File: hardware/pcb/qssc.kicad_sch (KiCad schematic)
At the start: 113 parts, among them J1 FT232RL, J10 USB-C, J11 Samtec LSHM-130, J2 5V Barrel, J3 SMA, J7 RESET, J8 MW_GATE, J9 JTAG, U1 XC7A35T-1CPG236C, U3 ADF4351BCPZ, U5 GVA-84+, U8 W25Q128JVSIQ, Y1 100MHz TCXO

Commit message: pcb: place 64-ch TIA/comparator front-end + 64-ch P-MOS emitter driver (Phase 1b, DRC 0/0/0)
Board widened 200 -> 210x140. 587 components: 16x TLV9004 TIA + 16x LMV339
comparator (8 cols @ 8mm in the right zone, sized to 2x the TSSOP-14 courtyard
half-extent 3.85mm -- the prior 6.5mm col spacing overlapped adjacent IC pads),
64x Rf/Cf TIA feedback, 64x Rpu comparator pull-up, MCP4725 threshold DAC +
I2C refs; 64x AO3401A P-MOS + 64x Re/64x Rg emitter driver + 8x 74HCT240 buffers
+ decoupling. Re/Rg y-staggered (same x-cols, +3mm y) -- the earlier x-interleave
shorted each Rg +5V pad into the next Re's em_drain pad (56 shorts). J3 SMA ->
x204 right edge, J8 -> (150,8).

ERC 0 errors (775 warnings: the intentional dangling 128 nets + off-grid pins).
DRC 0 violations / 0 unconnected. tests/test_pcb_drc.py passes. 128 nets still
dangle at the die until Phase 2 (FPGA CSG324).

Co-Authored-By: Claude Code <noreply@anthropic.com>
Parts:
- removed C66: 100nF, Capacitor_SMD:C_0603_1608Metric, symbol qssc:C
- removed J11: Samtec LSHM-130, Connector_Samtec:Samtec_LSHM-130-xx.x-x-DV-N_2x30_P0.50mm_Vertical, symbol qssc:Conn_02x30_Odd_Even
- removed R84: 47k, Resistor_SMD:R_0603_1608Metric, symbol qssc:R
- removed R85: 10k, Resistor_SMD:R_0603_1608Metric, symbol qssc:R
- added Cdac, Cref, Cub0, Cub1, Cub2, Cub3, Cub4, Cub5, Cub6, Cub7, Cuc0, Cuc1, Cuc10, Cuc11, Cuc12, Cuc13, Cuc14, Cuc15, Cuc2, Cuc3, Cuc4, Cuc5, Cuc6, Cuc7, Cuc8, Cuc9, Cut0, Cut1, Cut10, Cut11, Cut12, Cut13, Cut14, Cut15, Cut2, Cut3, Cut4, Cut5, Cut6, Cut7, Cut8, Cut9: 100nF, Capacitor_SMD:C_0603_1608Metric, symbol qssc:C
- added Cf0, Cf1, Cf10, Cf11, Cf12, Cf13, Cf14, Cf15, Cf16, Cf17, Cf18, Cf19, Cf2, Cf20, Cf21, Cf22, Cf23, Cf24, Cf25, Cf26, Cf27, Cf28, Cf29, Cf3, Cf30, Cf31, Cf32, Cf33, Cf34, Cf35, Cf36, Cf37, Cf38, Cf39, Cf4, Cf40, Cf41, Cf42, Cf43, Cf44, Cf45, Cf46, Cf47, Cf48, Cf49, Cf5, Cf50, Cf51, Cf52, Cf53, Cf54, Cf55, Cf56, Cf57, Cf58, Cf59, Cf6, Cf60, Cf61, Cf62, Cf63, Cf7, Cf8, Cf9: 1pF, Capacitor_SMD:C_0603_1608Metric, symbol qssc:C
- added Q0, Q1, Q10, Q11, Q12, Q13, Q14, Q15, Q16, Q17, Q18, Q19, Q2, Q20, Q21, Q22, Q23, Q24, Q25, Q26, Q27, Q28, Q29, Q3, Q30, Q31, Q32, Q33, Q34, Q35, Q36, Q37, Q38, Q39, Q4, Q40, Q41, Q42, Q43, Q44, Q45, Q46, Q47, Q48, Q49, Q5, Q50, Q51, Q52, Q53, Q54, Q55, Q56, Q57, Q58, Q59, Q6, Q60, Q61, Q62, Q63, Q7, Q8, Q9: AO3401A, Package_TO_SOT_SMD:SOT-23, symbol qssc:AO3401A
- added R_I2C_SCL, R_I2C_SDA: 4.7k, Resistor_SMD:R_0603_1608Metric, symbol qssc:R
- added Re0, Re1, Re10, Re11, Re12, Re13, Re14, Re15, Re16, Re17, Re18, Re19, Re2, Re20, Re21, Re22, Re23, Re24, Re25, Re26, Re27, Re28, Re29, Re3, Re30, Re31, Re32, Re33, Re34, Re35, Re36, Re37, Re38, Re39, Re4, Re40, Re41, Re42, Re43, Re44, Re45, Re46, Re47, Re48, Re49, Re5, Re50, Re51, Re52, Re53, Re54, Re55, Re56, Re57, Re58, Re59, Re6, Re60, Re61, Re62, Re63, Re7, Re8, Re9: 220R, Resistor_SMD:R_0603_1608Metric, symbol qssc:R
- added Rf0, Rf1, Rf10, Rf11, Rf12, Rf13, Rf14, Rf15, Rf16, Rf17, Rf18, Rf19, Rf2, Rf20, Rf21, Rf22, Rf23, Rf24, Rf25, Rf26, Rf27, Rf28, Rf29, Rf3, Rf30, Rf31, Rf32, Rf33, Rf34, Rf35, Rf36, Rf37, Rf38, Rf39, Rf4, Rf40, Rf41, Rf42, Rf43, Rf44, Rf45, Rf46, Rf47, Rf48, Rf49, Rf5, Rf50, Rf51, Rf52, Rf53, Rf54, Rf55, Rf56, Rf57, Rf58, Rf59, Rf6, Rf60, Rf61, Rf62, Rf63, Rf7, Rf8, Rf9: 1M, Resistor_SMD:R_0603_1608Metric, symbol qssc:R
- added Rg0, Rg1, Rg10, Rg11, Rg12, Rg13, Rg14, Rg15, Rg16, Rg17, Rg18, Rg19, Rg2, Rg20, Rg21, Rg22, Rg23, Rg24, Rg25, Rg26, Rg27, Rg28, Rg29, Rg3, Rg30, Rg31, Rg32, Rg33, Rg34, Rg35, Rg36, Rg37, Rg38, Rg39, Rg4, Rg40, Rg41, Rg42, Rg43, Rg44, Rg45, Rg46, Rg47, Rg48, Rg49, Rg5, Rg50, Rg51, Rg52, Rg53, Rg54, Rg55, Rg56, Rg57, Rg58, Rg59, Rg6, Rg60, Rg61, Rg62, Rg63, Rg7, Rg8, Rg9: 100k, Resistor_SMD:R_0603_1608Metric, symbol qssc:R
- added Rpu0, Rpu1, Rpu10, Rpu11, Rpu12, Rpu13, Rpu14, Rpu15, Rpu16, Rpu17, Rpu18, Rpu19, Rpu2, Rpu20, Rpu21, Rpu22, Rpu23, Rpu24, Rpu25, Rpu26, Rpu27, Rpu28, Rpu29, Rpu3, Rpu30, Rpu31, Rpu32, Rpu33, Rpu34, Rpu35, Rpu36, Rpu37, Rpu38, Rpu39, Rpu4, Rpu40, Rpu41, Rpu42, Rpu43, Rpu44, Rpu45, Rpu46, Rpu47, Rpu48, Rpu49, Rpu5, Rpu50, Rpu51, Rpu52, Rpu53, Rpu54, Rpu55, Rpu56, Rpu57, Rpu58, Rpu59, Rpu6, Rpu60, Rpu61, Rpu62, Rpu63, Rpu7, Rpu8, Rpu9, Rref1, Rref2: 10k, Resistor_SMD:R_0603_1608Metric, symbol qssc:R
- added UB0, UB1, UB2, UB3, UB4, UB5, UB6, UB7: 74HCT240, Package_SO:TSSOP-20_4.4x6.5mm_P0.65mm, symbol qssc:74HCT240
- added UC0, UC1, UC10, UC11, UC12, UC13, UC14, UC15, UC2, UC3, UC4, UC5, UC6, UC7, UC8, UC9: LMV339, Package_SO:SOIC-14_3.9x8.7mm_P1.27mm, symbol qssc:LMV339
- added UDAC: MCP4725, Package_TO_SOT_SMD:SOT-23-6, symbol qssc:MCP4725
- added UT0, UT1, UT10, UT11, UT12, UT13, UT14, UT15, UT2, UT3, UT4, UT5, UT6, UT7, UT8, UT9: TLV9004, Package_SO:TSSOP-14_4.4x5mm_P0.65mm, symbol qssc:TLV9004
- added Uchip: QSSC_Chip, qssc:QSSC_Chip, symbol qssc:QSSC_Chip
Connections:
- net +3V3: now also Cuc0.1, Cuc1.1, Cuc10.1, Cuc11.1, Cuc12.1, Cuc13.1, Cuc14.1, Cuc15.1, Cuc2.1, Cuc3.1, Cuc4.1, Cuc5.1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
- net +5V: now also Cub0.1, Cub1.1, Cub2.1, Cub3.1, Cub4.1, Cub5.1, Cub6.1, Cub7.1, Q0.2 (S), Q1.2 (S), Q10.2 (S), Q11.2 (S)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
- net GND: now also Cdac.2, Cref.2, Cub0.2, Cub1.2, Cub2.2, Cub3.2, Cub4.2, Cub5.2, Cub6.2, Cub7.2, Cuc0.2, Cuc1.2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; no longer U1.B13 (GND)
- removed net TIA_ADC: U1.A12 (TIA_ADC)
- new net DET_DIG0: Rpu0.1, UC0.1 (OUTA)
- new net DET_DIG1: Rpu1.1, UC0.6 (OUTB)
- new net DET_DIG10: Rpu10.1, UC2.8 (OUTC)
- new net DET_DIG11: Rpu11.1, UC2.11 (OUTD)
- new net DET_DIG12: Rpu12.1, UC3.1 (OUTA)
- new net DET_DIG13: Rpu13.1, UC3.6 (OUTB)
- new net DET_DIG14: Rpu14.1, UC3.8 (OUTC)
- new net DET_DIG15: Rpu15.1, UC3.11 (OUTD)
- new net DET_DIG16: Rpu16.1, UC4.1 (OUTA)
- new net DET_DIG17: Rpu17.1, UC4.6 (OUTB)
- new net DET_DIG18: Rpu18.1, UC4.8 (OUTC)
- new net DET_DIG19: Rpu19.1, UC4.11 (OUTD)
- new net DET_DIG2: Rpu2.1, UC0.8 (OUTC)
- new net DET_DIG20: Rpu20.1, UC5.1 (OUTA)
- new net DET_DIG21: Rpu21.1, UC5.6 (OUTB)
- new net DET_DIG22: Rpu22.1, UC5.8 (OUTC)
- new net DET_DIG23: Rpu23.1, UC5.11 (OUTD)
- new net DET_DIG24: Rpu24.1, UC6.1 (OUTA)
- new net DET_DIG25: Rpu25.1, UC6.6 (OUTB)
- new net DET_DIG26: Rpu26.1, UC6.8 (OUTC)
- new net DET_DIG27: Rpu27.1, UC6.11 (OUTD)
- new net DET_DIG28: Rpu28.1, UC7.1 (OUTA)
- new net DET_DIG29: Rpu29.1, UC7.6 (OUTB)
- new net DET_DIG3: Rpu3.1, UC0.11 (OUTD)
- new net DET_DIG30: Rpu30.1, UC7.8 (OUTC)
- new net DET_DIG31: Rpu31.1, UC7.11 (OUTD)
- new net DET_DIG32: Rpu32.1, UC8.1 (OUTA)
- new net DET_DIG33: Rpu33.1, UC8.6 (OUTB)
- new net DET_DIG34: Rpu34.1, UC8.8 (OUTC)
- new net DET_DIG35: Rpu35.1, UC8.11 (OUTD)
- new net DET_DIG36: Rpu36.1, UC9.1 (OUTA)
- new net DET_DIG37: Rpu37.1, UC9.6 (OUTB)
- new net DET_DIG38: Rpu38.1, UC9.8 (OUTC)
- new net DET_DIG39: Rpu39.1, UC9.11 (OUTD)
- new net DET_DIG4: Rpu4.1, UC1.1 (OUTA)
- new net DET_DIG40: Rpu40.1, UC10.1 (OUTA)
- new net DET_DIG41: Rpu41.1, UC10.6 (OUTB)
- new net DET_DIG42: Rpu42.1, UC10.8 (OUTC)
- new net DET_DIG43: Rpu43.1, UC10.11 (OUTD)
- new net DET_DIG44: Rpu44.1, UC11.1 (OUTA)
- new net DET_DIG45: Rpu45.1, UC11.6 (OUTB)
- new net DET_DIG46: Rpu46.1, UC11.8 (OUTC)
- new net DET_DIG47: Rpu47.1, UC11.11 (OUTD)
- new net DET_DIG48: Rpu48.1, UC12.1 (OUTA)
- new net DET_DIG49: Rpu49.1, UC12.6 (OUTB)
- new net DET_DIG5: Rpu5.1, UC1.6 (OUTB)
- new net DET_DIG50: Rpu50.1, UC12.8 (OUTC)
- new net DET_DIG51: Rpu51.1, UC12.11 (OUTD)
- new net DET_DIG52: Rpu52.1, UC13.1 (OUTA)
- new net DET_DIG53: Rpu53.1, UC13.6 (OUTB)
- new net DET_DIG54: Rpu54.1, UC13.8 (OUTC)
- new net DET_DIG55: Rpu55.1, UC13.11 (OUTD)
- new net DET_DIG56: Rpu56.1, UC14.1 (OUTA)
- new net DET_DIG57: Rpu57.1, UC14.6 (OUTB)
- new net DET_DIG58: Rpu58.1, UC14.8 (OUTC)
- new net DET_DIG59: Rpu59.1, UC14.11 (OUTD)
- new net DET_DIG6: Rpu6.1, UC1.8 (OUTC)
- new net DET_DIG60: Rpu60.1, UC15.1 (OUTA)
- new net DET_DIG61: Rpu61.1, UC15.6 (OUTB)
- new net DET_DIG62: Rpu62.1, UC15.8 (OUTC)
- new net DET_DIG63: Rpu63.1, UC15.11 (OUTD)
- new net DET_DIG7: Rpu7.1, UC1.11 (OUTD)
- new net DET_DIG8: Rpu8.1, UC2.1 (OUTA)
- new net DET_DIG9: Rpu9.1, UC2.6 (OUTB)
- new net DET_IN0: Cf0.1, Rf0.1, UT0.2 (INA-), Uchip.DET0
- new net DET_IN1: Cf1.1, Rf1.1, UT0.6 (INB-), Uchip.DET1
- new net DET_IN10: Cf10.1, Rf10.1, UT2.9 (INC-), Uchip.DET10
- new net DET_IN11: Cf11.1, Rf11.1, UT2.13 (IND-), Uchip.DET11
- new net DET_IN12: Cf12.1, Rf12.1, UT3.2 (INA-), Uchip.DET12
- new net DET_IN13: Cf13.1, Rf13.1, UT3.6 (INB-), Uchip.DET13
- new net DET_IN14: Cf14.1, Rf14.1, UT3.9 (INC-), Uchip.DET14
- new net DET_IN15: Cf15.1, Rf15.1, UT3.13 (IND-), Uchip.DET15
- new net DET_IN16: Cf16.1, Rf16.1, UT4.2 (INA-), Uchip.DET16
- new net DET_IN17: Cf17.1, Rf17.1, UT4.6 (INB-), Uchip.DET17
- new net DET_IN18: Cf18.1, Rf18.1, UT4.9 (INC-), Uchip.DET18
- new net DET_IN19: Cf19.1, Rf19.1, UT4.13 (IND-), Uchip.DET19
- new net DET_IN2: Cf2.1, Rf2.1, UT0.9 (INC-), Uchip.DET2
- new net DET_IN20: Cf20.1, Rf20.1, UT5.2 (INA-), Uchip.DET20
- new net DET_IN21: Cf21.1, Rf21.1, UT5.6 (INB-), Uchip.DET21
- new net DET_IN22: Cf22.1, Rf22.1, UT5.9 (INC-), Uchip.DET22
- new net DET_IN23: Cf23.1, Rf23.1, UT5.13 (IND-), Uchip.DET23
- new net DET_IN24: Cf24.1, Rf24.1, UT6.2 (INA-), Uchip.DET24
- new net DET_IN25: Cf25.1, Rf25.1, UT6.6 (INB-), Uchip.DET25
- new net DET_IN26: Cf26.1, Rf26.1, UT6.9 (INC-), Uchip.DET26
- new net DET_IN27: Cf27.1, Rf27.1, UT6.13 (IND-), Uchip.DET27
- new net DET_IN28: Cf28.1, Rf28.1, UT7.2 (INA-), Uchip.DET28
- new net DET_IN29: Cf29.1, Rf29.1, UT7.6 (INB-), Uchip.DET29
- new net DET_IN3: Cf3.1, Rf3.1, UT0.13 (IND-), Uchip.DET3
- new net DET_IN30: Cf30.1, Rf30.1, UT7.9 (INC-), Uchip.DET30
- new net DET_IN31: Cf31.1, Rf31.1, UT7.13 (IND-), Uchip.DET31
- new net DET_IN32: Cf32.1, Rf32.1, UT8.2 (INA-), Uchip.DET32
- new net DET_IN33: Cf33.1, Rf33.1, UT8.6 (INB-), Uchip.DET33
- new net DET_IN34: Cf34.1, Rf34.1, UT8.9 (INC-), Uchip.DET34
- new net DET_IN35: Cf35.1, Rf35.1, UT8.13 (IND-), Uchip.DET35
- new net DET_IN36: Cf36.1, Rf36.1, UT9.2 (INA-), Uchip.DET36
- new net DET_IN37: Cf37.1, Rf37.1, UT9.6 (INB-), Uchip.DET37
- new net DET_IN38: Cf38.1, Rf38.1, UT9.9 (INC-), Uchip.DET38
- new net DET_IN39: Cf39.1, Rf39.1, UT9.13 (IND-), Uchip.DET39
- new net DET_IN4: Cf4.1, Rf4.1, UT1.2 (INA-), Uchip.DET4
- new net DET_IN40: Cf40.1, Rf40.1, UT10.2 (INA-), Uchip.DET40
- new net DET_IN41: Cf41.1, Rf41.1, UT10.6 (INB-), Uchip.DET41
- new net DET_IN42: Cf42.1, Rf42.1, UT10.9 (INC-), Uchip.DET42
- new net DET_IN43: Cf43.1, Rf43.1, UT10.13 (IND-), Uchip.DET43
- new net DET_IN44: Cf44.1, Rf44.1, UT11.2 (INA-), Uchip.DET44
- new net DET_IN45: Cf45.1, Rf45.1, UT11.6 (INB-), Uchip.DET45
- new net DET_IN46: Cf46.1, Rf46.1, UT11.9 (INC-), Uchip.DET46
- new net DET_IN47: Cf47.1, Rf47.1, UT11.13 (IND-), Uchip.DET47
- new net DET_IN48: Cf48.1, Rf48.1, UT12.2 (INA-), Uchip.DET48
- new net DET_IN49: Cf49.1, Rf49.1, UT12.6 (INB-), Uchip.DET49
- new net DET_IN5: Cf5.1, Rf5.1, UT1.6 (INB-), Uchip.DET5
- new net DET_IN50: Cf50.1, Rf50.1, UT12.9 (INC-), Uchip.DET50
- new net DET_IN51: Cf51.1, Rf51.1, UT12.13 (IND-), Uchip.DET51
- new net DET_IN52: Cf52.1, Rf52.1, UT13.2 (INA-), Uchip.DET52
- new net DET_IN53: Cf53.1, Rf53.1, UT13.6 (INB-), Uchip.DET53
- new net DET_IN54: Cf54.1, Rf54.1, UT13.9 (INC-), Uchip.DET54
- new net DET_IN55: Cf55.1, Rf55.1, UT13.13 (IND-), Uchip.DET55
- new net DET_IN56: Cf56.1, Rf56.1, UT14.2 (INA-), Uchip.DET56
- new net DET_IN57: Cf57.1, Rf57.1, UT14.6 (INB-), Uchip.DET57
- new net DET_IN58: Cf58.1, Rf58.1, UT14.9 (INC-), Uchip.DET58
- new net DET_IN59: Cf59.1, Rf59.1, UT14.13 (IND-), Uchip.DET59
- new net DET_IN6: Cf6.1, Rf6.1, UT1.9 (INC-), Uchip.DET6
- new net DET_IN60: Cf60.1, Rf60.1, UT15.2 (INA-), Uchip.DET60
- new net DET_IN61: Cf61.1, Rf61.1, UT15.6 (INB-), Uchip.DET61
- new net DET_IN62: Cf62.1, Rf62.1, UT15.9 (INC-), Uchip.DET62
- new net DET_IN63: Cf63.1, Rf63.1, UT15.13 (IND-), Uchip.DET63
- new net DET_IN7: Cf7.1, Rf7.1, UT1.13 (IND-), Uchip.DET7
- new net DET_IN8: Cf8.1, Rf8.1, UT2.2 (INA-), Uchip.DET8
- new net DET_IN9: Cf9.1, Rf9.1, UT2.6 (INB-), Uchip.DET9
- new net DET_REF: Cref.1, Rref1.2, Rref2.1, UT0.10 (INC+), UT0.12 (IND+), UT0.3 (INA+), UT0.5 (INB+), UT1.10 (INC+), UT1.12 (IND+), UT1.3 (INA+), UT1.5 (INB+), UT10.10 (INC+)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
- new net DET_THR: Cdac.1, UC0.13 (IND-), UC0.2 (INA-), UC0.4 (INB-), UC0.9 (INC-), UC1.13 (IND-), UC1.2 (INA-), UC1.4 (INB-), UC1.9 (INC-), UC10.13 (IND-), UC10.2 (INA-), UC10.4 (INB-)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
- new net DET_TIA0: Cf0.2, Rf0.2, UC0.3 (INA+), UT0.1 (OUTA)
- new net DET_TIA1: Cf1.2, Rf1.2, UC0.5 (INB+), UT0.7 (OUTB)
- new net DET_TIA10: Cf10.2, Rf10.2, UC2.10 (INC+), UT2.8 (OUTC)
- new net DET_TIA11: Cf11.2, Rf11.2, UC2.12 (IND+), UT2.14 (OUTD)
- new net DET_TIA12: Cf12.2, Rf12.2, UC3.3 (INA+), UT3.1 (OUTA)
- new net DET_TIA13: Cf13.2, Rf13.2, UC3.5 (INB+), UT3.7 (OUTB)
- new net DET_TIA14: Cf14.2, Rf14.2, UC3.10 (INC+), UT3.8 (OUTC)
- new net DET_TIA15: Cf15.2, Rf15.2, UC3.12 (IND+), UT3.14 (OUTD)
- new net DET_TIA16: Cf16.2, Rf16.2, UC4.3 (INA+), UT4.1 (OUTA)
- new net DET_TIA17: Cf17.2, Rf17.2, UC4.5 (INB+), UT4.7 (OUTB)
- new net DET_TIA18: Cf18.2, Rf18.2, UC4.10 (INC+), UT4.8 (OUTC)
- new net DET_TIA19: Cf19.2, Rf19.2, UC4.12 (IND+), UT4.14 (OUTD)
- new net DET_TIA2: Cf2.2, Rf2.2, UC0.10 (INC+), UT0.8 (OUTC)
- new net DET_TIA20: Cf20.2, Rf20.2, UC5.3 (INA+), UT5.1 (OUTA)
- new net DET_TIA21: Cf21.2, Rf21.2, UC5.5 (INB+), UT5.7 (OUTB)
- new net DET_TIA22: Cf22.2, Rf22.2, UC5.10 (INC+), UT5.8 (OUTC)
- new net DET_TIA23: Cf23.2, Rf23.2, UC5.12 (IND+), UT5.14 (OUTD)
- new net DET_TIA24: Cf24.2, Rf24.2, UC6.3 (INA+), UT6.1 (OUTA)
- new net DET_TIA25: Cf25.2, Rf25.2, UC6.5 (INB+), UT6.7 (OUTB)
- new net DET_TIA26: Cf26.2, Rf26.2, UC6.10 (INC+), UT6.8 (OUTC)
- new net DET_TIA27: Cf27.2, Rf27.2, UC6.12 (IND+), UT6.14 (OUTD)
- new net DET_TIA28: Cf28.2, Rf28.2, UC7.3 (INA+), UT7.1 (OUTA)
- new net DET_TIA29: Cf29.2, Rf29.2, UC7.5 (INB+), UT7.7 (OUTB)
- new net DET_TIA3: Cf3.2, Rf3.2, UC0.12 (IND+), UT0.14 (OUTD)
- new net DET_TIA30: Cf30.2, Rf30.2, UC7.10 (INC+), UT7.8 (OUTC)
- new net DET_TIA31: Cf31.2, Rf31.2, UC7.12 (IND+), UT7.14 (OUTD)
- new net DET_TIA32: Cf32.2, Rf32.2, UC8.3 (INA+), UT8.1 (OUTA)
- new net DET_TIA33: Cf33.2, Rf33.2, UC8.5 (INB+), UT8.7 (OUTB)
- new net DET_TIA34: Cf34.2, Rf34.2, UC8.10 (INC+), UT8.8 (OUTC)
- new net DET_TIA35: Cf35.2, Rf35.2, UC8.12 (IND+), UT8.14 (OUTD)
- new net DET_TIA36: Cf36.2, Rf36.2, UC9.3 (INA+), UT9.1 (OUTA)
- new net DET_TIA37: Cf37.2, Rf37.2, UC9.5 (INB+), UT9.7 (OUTB)
- new net DET_TIA38: Cf38.2, Rf38.2, UC9.10 (INC+), UT9.8 (OUTC)
- new net DET_TIA39: Cf39.2, Rf39.2, UC9.12 (IND+), UT9.14 (OUTD)
- new net DET_TIA4: Cf4.2, Rf4.2, UC1.3 (INA+), UT1.1 (OUTA)
- new net DET_TIA40: Cf40.2, Rf40.2, UC10.3 (INA+), UT10.1 (OUTA)
- new net DET_TIA41: Cf41.2, Rf41.2, UC10.5 (INB+), UT10.7 (OUTB)
- new net DET_TIA42: Cf42.2, Rf42.2, UC10.10 (INC+), UT10.8 (OUTC)
- new net DET_TIA43: Cf43.2, Rf43.2, UC10.12 (IND+), UT10.14 (OUTD)
- new net DET_TIA44: Cf44.2, Rf44.2, UC11.3 (INA+), UT11.1 (OUTA)
- new net DET_TIA45: Cf45.2, Rf45.2, UC11.5 (INB+), UT11.7 (OUTB)
- new net DET_TIA46: Cf46.2, Rf46.2, UC11.10 (INC+), UT11.8 (OUTC)
- new net DET_TIA47: Cf47.2, Rf47.2, UC11.12 (IND+), UT11.14 (OUTD)
- new net DET_TIA48: Cf48.2, Rf48.2, UC12.3 (INA+), UT12.1 (OUTA)
- new net DET_TIA49: Cf49.2, Rf49.2, UC12.5 (INB+), UT12.7 (OUTB)
- new net DET_TIA5: Cf5.2, Rf5.2, UC1.5 (INB+), UT1.7 (OUTB)
- new net DET_TIA50: Cf50.2, Rf50.2, UC12.10 (INC+), UT12.8 (OUTC)
- new net DET_TIA51: Cf51.2, Rf51.2, UC12.12 (IND+), UT12.14 (OUTD)
- new net DET_TIA52: Cf52.2, Rf52.2, UC13.3 (INA+), UT13.1 (OUTA)
- new net DET_TIA53: Cf53.2, Rf53.2, UC13.5 (INB+), UT13.7 (OUTB)
- new net DET_TIA54: Cf54.2, Rf54.2, UC13.10 (INC+), UT13.8 (OUTC)
- new net DET_TIA55: Cf55.2, Rf55.2, UC13.12 (IND+), UT13.14 (OUTD)
- new net DET_TIA56: Cf56.2, Rf56.2, UC14.3 (INA+), UT14.1 (OUTA)
- new net DET_TIA57: Cf57.2, Rf57.2, UC14.5 (INB+), UT14.7 (OUTB)
- new net DET_TIA58: Cf58.2, Rf58.2, UC14.10 (INC+), UT14.8 (OUTC)
- new net DET_TIA59: Cf59.2, Rf59.2, UC14.12 (IND+), UT14.14 (OUTD)
- new net DET_TIA6: Cf6.2, Rf6.2, UC1.10 (INC+), UT1.8 (OUTC)
- new net DET_TIA60: Cf60.2, Rf60.2, UC15.3 (INA+), UT15.1 (OUTA)
- new net DET_TIA61: Cf61.2, Rf61.2, UC15.5 (INB+), UT15.7 (OUTB)
- new net DET_TIA62: Cf62.2, Rf62.2, UC15.10 (INC+), UT15.8 (OUTC)
- new net DET_TIA63: Cf63.2, Rf63.2, UC15.12 (IND+), UT15.14 (OUTD)
- new net DET_TIA7: Cf7.2, Rf7.2, UC1.12 (IND+), UT1.14 (OUTD)
- new net DET_TIA8: Cf8.2, Rf8.2, UC2.3 (INA+), UT2.1 (OUTA)
- new net DET_TIA9: Cf9.2, Rf9.2, UC2.5 (INB+), UT2.7 (OUTB)
- new net EM_DRV0: UB0.2 (1A0)
- new net EM_DRV1: UB0.4 (1A1)
- new net EM_DRV10: UB1.6 (1A2)
- new net EM_DRV11: UB1.8 (1A3)
- new net EM_DRV12: UB1.17 (2A0)
- new net EM_DRV13: UB1.15 (2A1)
- new net EM_DRV14: UB1.13 (2A2)
- new net EM_DRV15: UB1.11 (2A3)
- new net EM_DRV16: UB2.2 (1A0)
- new net EM_DRV17: UB2.4 (1A1)
- new net EM_DRV18: UB2.6 (1A2)
- new net EM_DRV19: UB2.8 (1A3)
- new net EM_DRV2: UB0.6 (1A2)
- new net EM_DRV20: UB2.17 (2A0)
- new net EM_DRV21: UB2.15 (2A1)
- new net EM_DRV22: UB2.13 (2A2)
- new net EM_DRV23: UB2.11 (2A3)
- new net EM_DRV24: UB3.2 (1A0)
- new net EM_DRV25: UB3.4 (1A1)
- new net EM_DRV26: UB3.6 (1A2)
- new net EM_DRV27: UB3.8 (1A3)
- new net EM_DRV28: UB3.17 (2A0)
- new net EM_DRV29: UB3.15 (2A1)
- new net EM_DRV3: UB0.8 (1A3)
- new net EM_DRV30: UB3.13 (2A2)
- new net EM_DRV31: UB3.11 (2A3)
- new net EM_DRV32: UB4.2 (1A0)
- new net EM_DRV33: UB4.4 (1A1)
- new net EM_DRV34: UB4.6 (1A2)
- new net EM_DRV35: UB4.8 (1A3)
- new net EM_DRV36: UB4.17 (2A0)
- new net EM_DRV37: UB4.15 (2A1)
- new net EM_DRV38: UB4.13 (2A2)
- new net EM_DRV39: UB4.11 (2A3)
- new net EM_DRV4: UB0.17 (2A0)
- new net EM_DRV40: UB5.2 (1A0)
- new net EM_DRV41: UB5.4 (1A1)
- new net EM_DRV42: UB5.6 (1A2)
- new net EM_DRV43: UB5.8 (1A3)
- new net EM_DRV44: UB5.17 (2A0)
- new net EM_DRV45: UB5.15 (2A1)
- new net EM_DRV46: UB5.13 (2A2)
- new net EM_DRV47: UB5.11 (2A3)
- new net EM_DRV48: UB6.2 (1A0)
- new net EM_DRV49: UB6.4 (1A1)
- new net EM_DRV5: UB0.15 (2A1)
- new net EM_DRV50: UB6.6 (1A2)
- new net EM_DRV51: UB6.8 (1A3)
- new net EM_DRV52: UB6.17 (2A0)
- new net EM_DRV53: UB6.15 (2A1)
- new net EM_DRV54: UB6.13 (2A2)
- new net EM_DRV55: UB6.11 (2A3)
- new net EM_DRV56: UB7.2 (1A0)
- new net EM_DRV57: UB7.4 (1A1)
- new net EM_DRV58: UB7.6 (1A2)
- new net EM_DRV59: UB7.8 (1A3)
- new net EM_DRV6: UB0.13 (2A2)
- new net EM_DRV60: UB7.17 (2A0)
- new net EM_DRV61: UB7.15 (2A1)
- new net EM_DRV62: UB7.13 (2A2)
- new net EM_DRV63: UB7.11 (2A3)
- new net EM_DRV7: UB0.11 (2A3)
- new net EM_DRV8: UB1.2 (1A0)
- new net EM_DRV9: UB1.4 (1A1)
- new net I2C_SCL: R_I2C_SCL.1, UDAC.5 (SCL)
- new net I2C_SDA: R_I2C_SDA.1, UDAC.4 (SDA)
- new net em_drain0: Q0.3 (D), Re0.1
- new net em_drain1: Q1.3 (D), Re1.1
- new net em_drain10: Q10.3 (D), Re10.1
- new net em_drain11: Q11.3 (D), Re11.1
- new net em_drain12: Q12.3 (D), Re12.1
- new net em_drain13: Q13.3 (D), Re13.1
- new net em_drain14: Q14.3 (D), Re14.1
- new net em_drain15: Q15.3 (D), Re15.1
- new net em_drain16: Q16.3 (D), Re16.1
- new net em_drain17: Q17.3 (D), Re17.1
- new net em_drain18: Q18.3 (D), Re18.1
- new net em_drain19: Q19.3 (D), Re19.1
- new net em_drain2: Q2.3 (D), Re2.1
- new net em_drain20: Q20.3 (D), Re20.1
- new net em_drain21: Q21.3 (D), Re21.1
- new net em_drain22: Q22.3 (D), Re22.1
- new net em_drain23: Q23.3 (D), Re23.1
- new net em_drain24: Q24.3 (D), Re24.1
- new net em_drain25: Q25.3 (D), Re25.1
- new net em_drain26: Q26.3 (D), Re26.1
- new net em_drain27: Q27.3 (D), Re27.1
- new net em_drain28: Q28.3 (D), Re28.1
- new net em_drain29: Q29.3 (D), Re29.1
- new net em_drain3: Q3.3 (D), Re3.1
- new net em_drain30: Q30.3 (D), Re30.1
- new net em_drain31: Q31.3 (D), Re31.1
- new net em_drain32: Q32.3 (D), Re32.1
- new net em_drain33: Q33.3 (D), Re33.1
- new net em_drain34: Q34.3 (D), Re34.1
- new net em_drain35: Q35.3 (D), Re35.1
- new net em_drain36: Q36.3 (D), Re36.1
- new net em_drain37: Q37.3 (D), Re37.1
- new net em_drain38: Q38.3 (D), Re38.1
- new net em_drain39: Q39.3 (D), Re39.1
- new net em_drain4: Q4.3 (D), Re4.1
- new net em_drain40: Q40.3 (D), Re40.1
- new net em_drain41: Q41.3 (D), Re41.1
- new net em_drain42: Q42.3 (D), Re42.1
- new net em_drain43: Q43.3 (D), Re43.1
- new net em_drain44: Q44.3 (D), Re44.1
- new net em_drain45: Q45.3 (D), Re45.1
- new net em_drain46: Q46.3 (D), Re46.1
- new net em_drain47: Q47.3 (D), Re47.1
- new net em_drain48: Q48.3 (D), Re48.1
- new net em_drain49: Q49.3 (D), Re49.1
- new net em_drain5: Q5.3 (D), Re5.1
- new net em_drain50: Q50.3 (D), Re50.1
- new net em_drain51: Q51.3 (D), Re51.1
- new net em_drain52: Q52.3 (D), Re52.1
- new net em_drain53: Q53.3 (D), Re53.1
- new net em_drain54: Q54.3 (D), Re54.1
- new net em_drain55: Q55.3 (D), Re55.1
- new net em_drain56: Q56.3 (D), Re56.1
- new net em_drain57: Q57.3 (D), Re57.1
- new net em_drain58: Q58.3 (D), Re58.1
- new net em_drain59: Q59.3 (D), Re59.1
- new net em_drain6: Q6.3 (D), Re6.1
- new net em_drain60: Q60.3 (D), Re60.1
- new net em_drain61: Q61.3 (D), Re61.1
- new net em_drain62: Q62.3 (D), Re62.1
- new net em_drain63: Q63.3 (D), Re63.1
- new net em_drain7: Q7.3 (D), Re7.1
- new net em_drain8: Q8.3 (D), Re8.1
- new net em_drain9: Q9.3 (D), Re9.1
- new net em_gate0: Q0.1 (G), Rg0.1, UB0.18 (1Y0)
- new net em_gate1: Q1.1 (G), Rg1.1, UB0.16 (1Y1)
- new net em_gate10: Q10.1 (G), Rg10.1, UB1.14 (1Y2)
- new net em_gate11: Q11.1 (G), Rg11.1, UB1.12 (1Y3)
- new net em_gate12: Q12.1 (G), Rg12.1, UB1.3 (2Y0)
- new net em_gate13: Q13.1 (G), Rg13.1, UB1.5 (2Y1)
- new net em_gate14: Q14.1 (G), Rg14.1, UB1.7 (2Y2)
- new net em_gate15: Q15.1 (G), Rg15.1, UB1.9 (2Y3)
- new net em_gate16: Q16.1 (G), Rg16.1, UB2.18 (1Y0)
- new net em_gate17: Q17.1 (G), Rg17.1, UB2.16 (1Y1)
- new net em_gate18: Q18.1 (G), Rg18.1, UB2.14 (1Y2)
- new net em_gate19: Q19.1 (G), Rg19.1, UB2.12 (1Y3)
- new net em_gate2: Q2.1 (G), Rg2.1, UB0.14 (1Y2)
- new net em_gate20: Q20.1 (G), Rg20.1, UB2.3 (2Y0)
- new net em_gate21: Q21.1 (G), Rg21.1, UB2.5 (2Y1)
- new net em_gate22: Q22.1 (G), Rg22.1, UB2.7 (2Y2)
- new net em_gate23: Q23.1 (G), Rg23.1, UB2.9 (2Y3)
- new net em_gate24: Q24.1 (G), Rg24.1, UB3.18 (1Y0)
- new net em_gate25: Q25.1 (G), Rg25.1, UB3.16 (1Y1)
- new net em_gate26: Q26.1 (G), Rg26.1, UB3.14 (1Y2)
- new net em_gate27: Q27.1 (G), Rg27.1, UB3.12 (1Y3)
- new net em_gate28: Q28.1 (G), Rg28.1, UB3.3 (2Y0)
- new net em_gate29: Q29.1 (G), Rg29.1, UB3.5 (2Y1)
- new net em_gate3: Q3.1 (G), Rg3.1, UB0.12 (1Y3)
- new net em_gate30: Q30.1 (G), Rg30.1, UB3.7 (2Y2)
- new net em_gate31: Q31.1 (G), Rg31.1, UB3.9 (2Y3)
- new net em_gate32: Q32.1 (G), Rg32.1, UB4.18 (1Y0)
- new net em_gate33: Q33.1 (G), Rg33.1, UB4.16 (1Y1)
- new net em_gate34: Q34.1 (G), Rg34.1, UB4.14 (1Y2)
- new net em_gate35: Q35.1 (G), Rg35.1, UB4.12 (1Y3)
- new net em_gate36: Q36.1 (G), Rg36.1, UB4.3 (2Y0)
- new net em_gate37: Q37.1 (G), Rg37.1, UB4.5 (2Y1)
- new net em_gate38: Q38.1 (G), Rg38.1, UB4.7 (2Y2)
- new net em_gate39: Q39.1 (G), Rg39.1, UB4.9 (2Y3)
- new net em_gate4: Q4.1 (G), Rg4.1, UB0.3 (2Y0)
- new net em_gate40: Q40.1 (G), Rg40.1, UB5.18 (1Y0)
- new net em_gate41: Q41.1 (G), Rg41.1, UB5.16 (1Y1)
- new net em_gate42: Q42.1 (G), Rg42.1, UB5.14 (1Y2)
- new net em_gate43: Q43.1 (G), Rg43.1, UB5.12 (1Y3)
- new net em_gate44: Q44.1 (G), Rg44.1, UB5.3 (2Y0)
- new net em_gate45: Q45.1 (G), Rg45.1, UB5.5 (2Y1)
- new net em_gate46: Q46.1 (G), Rg46.1, UB5.7 (2Y2)
- new net em_gate47: Q47.1 (G), Rg47.1, UB5.9 (2Y3)
- new net em_gate48: Q48.1 (G), Rg48.1, UB6.18 (1Y0)
- new net em_gate49: Q49.1 (G), Rg49.1, UB6.16 (1Y1)
- new net em_gate5: Q5.1 (G), Rg5.1, UB0.5 (2Y1)
- new net em_gate50: Q50.1 (G), Rg50.1, UB6.14 (1Y2)
- new net em_gate51: Q51.1 (G), Rg51.1, UB6.12 (1Y3)
- new net em_gate52: Q52.1 (G), Rg52.1, UB6.3 (2Y0)
- new net em_gate53: Q53.1 (G), Rg53.1, UB6.5 (2Y1)
- new net em_gate54: Q54.1 (G), Rg54.1, UB6.7 (2Y2)
- new net em_gate55: Q55.1 (G), Rg55.1, UB6.9 (2Y3)
- new net em_gate56: Q56.1 (G), Rg56.1, UB7.18 (1Y0)
- new net em_gate57: Q57.1 (G), Rg57.1, UB7.16 (1Y1)
- new net em_gate58: Q58.1 (G), Rg58.1, UB7.14 (1Y2)
- new net em_gate59: Q59.1 (G), Rg59.1, UB7.12 (1Y3)
- new net em_gate6: Q6.1 (G), Rg6.1, UB0.7 (2Y2)
- new net em_gate60: Q60.1 (G), Rg60.1, UB7.3 (2Y0)
- new net em_gate61: Q61.1 (G), Rg61.1, UB7.5 (2Y1)
- new net em_gate62: Q62.1 (G), Rg62.1, UB7.7 (2Y2)
- new net em_gate63: Q63.1 (G), Rg63.1, UB7.9 (2Y3)
- new net em_gate7: Q7.1 (G), Rg7.1, UB0.9 (2Y3)
- new net em_gate8: Q8.1 (G), Rg8.1, UB1.18 (1Y0)
- new net em_gate9: Q9.1 (G), Rg9.1, UB1.16 (1Y1)
- new net emitter_anode0: Re0.2, Uchip.EM0
- new net emitter_anode1: Re1.2, Uchip.EM1
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
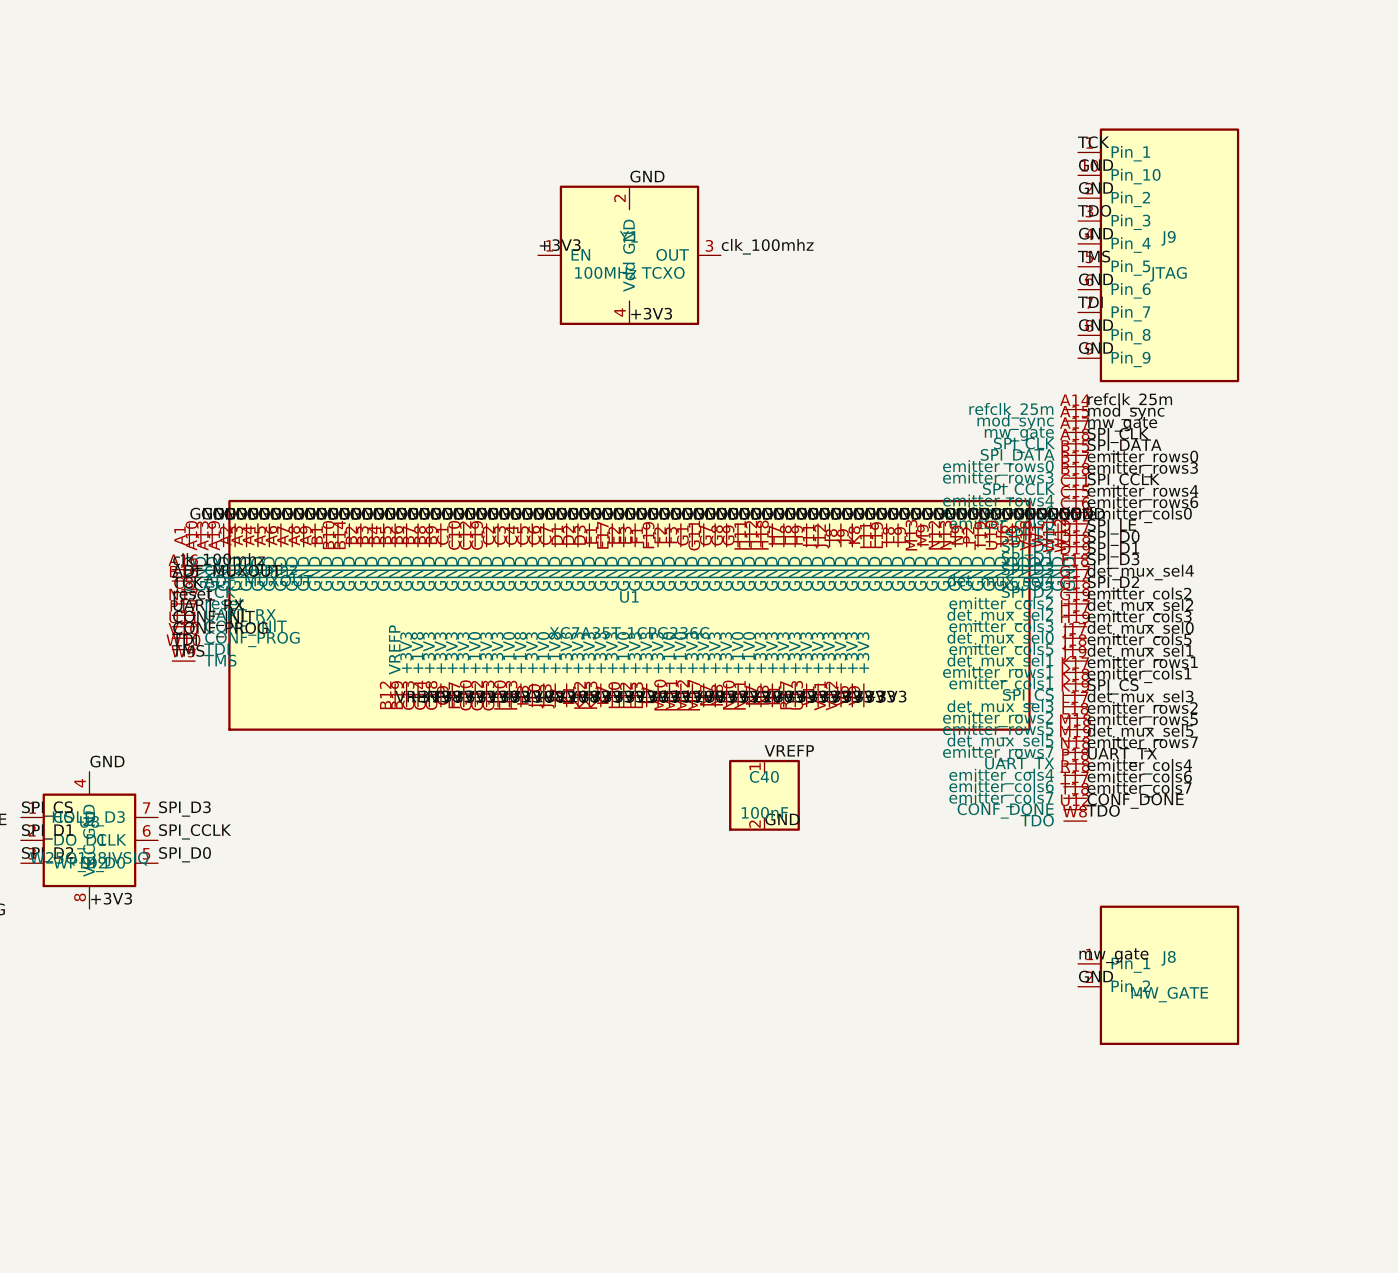
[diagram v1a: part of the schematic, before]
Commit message: phase 2: bump FPGA CPG236 -> CSG324, wire 128 parallel nets
The parallel 64-ch readout (64 DET_DIG inputs) + 64-ch emitter drive
(64 EM_DRV outputs) + 13 control nets need ~141 user IO, exceeding the
CPG236's ~125. CSG324 has 215 user IO (324 balls, 0.8 mm BGA, courtyard
+-8.5 mm -- FPGA placement (128,55) unchanged, clears die/front-end).

- tools/gen_fpga_ballmap_csg324.py: parse XC7A35T-CSG324 symbol (324
  pads); classify power from pin names; side-assign 64 DET_DIG -> right
  edge (toward comparator front-end x>=144), 64 EM_DRV -> bottom edge
  (toward 74HCT240 buffers y>=80), clocks on MRCC balls. 99 power balls
  netted (no floating GND/supply). Drops det_mux_sel/emitter_rows/cols.
- tools/gen_qssc_kicad.py: load CSG324 map; fpga_net_map/fpga_pin_list
  net 141 signals (64 DET_DIG left column, 64 EM_DRV + control right);
  symbol XC7A35T_CSG324 + footprint Package_BGA:Xilinx_CSG324.
- tools/gen_xdc.py: parallel XDC -- det_in[63:0], emitter_en[63:0],
  i2c_sda/scl (MCP4725 threshold DAC); remove MUX/row/col/XADC.
- Regenerated board: ERC 0 errors (625 warnings -- unused FT232/USB-C/
  ADF4351 pins + off-grid die pads), DRC 0 violations / 0 footprint errors.
  256 FPGA balls netted, all 128 parallel nets wired FPGA<->front-end.

Phase 3 (RTL serial->parallel) will align top_level.v ports to the new
XDC (det_in/emitter_en/i2c_sda/scl); check_xdc_ports.py mismatch is the
known in-flight state until then.

Co-Authored-By: Claude Code <noreply@anthropic.com>
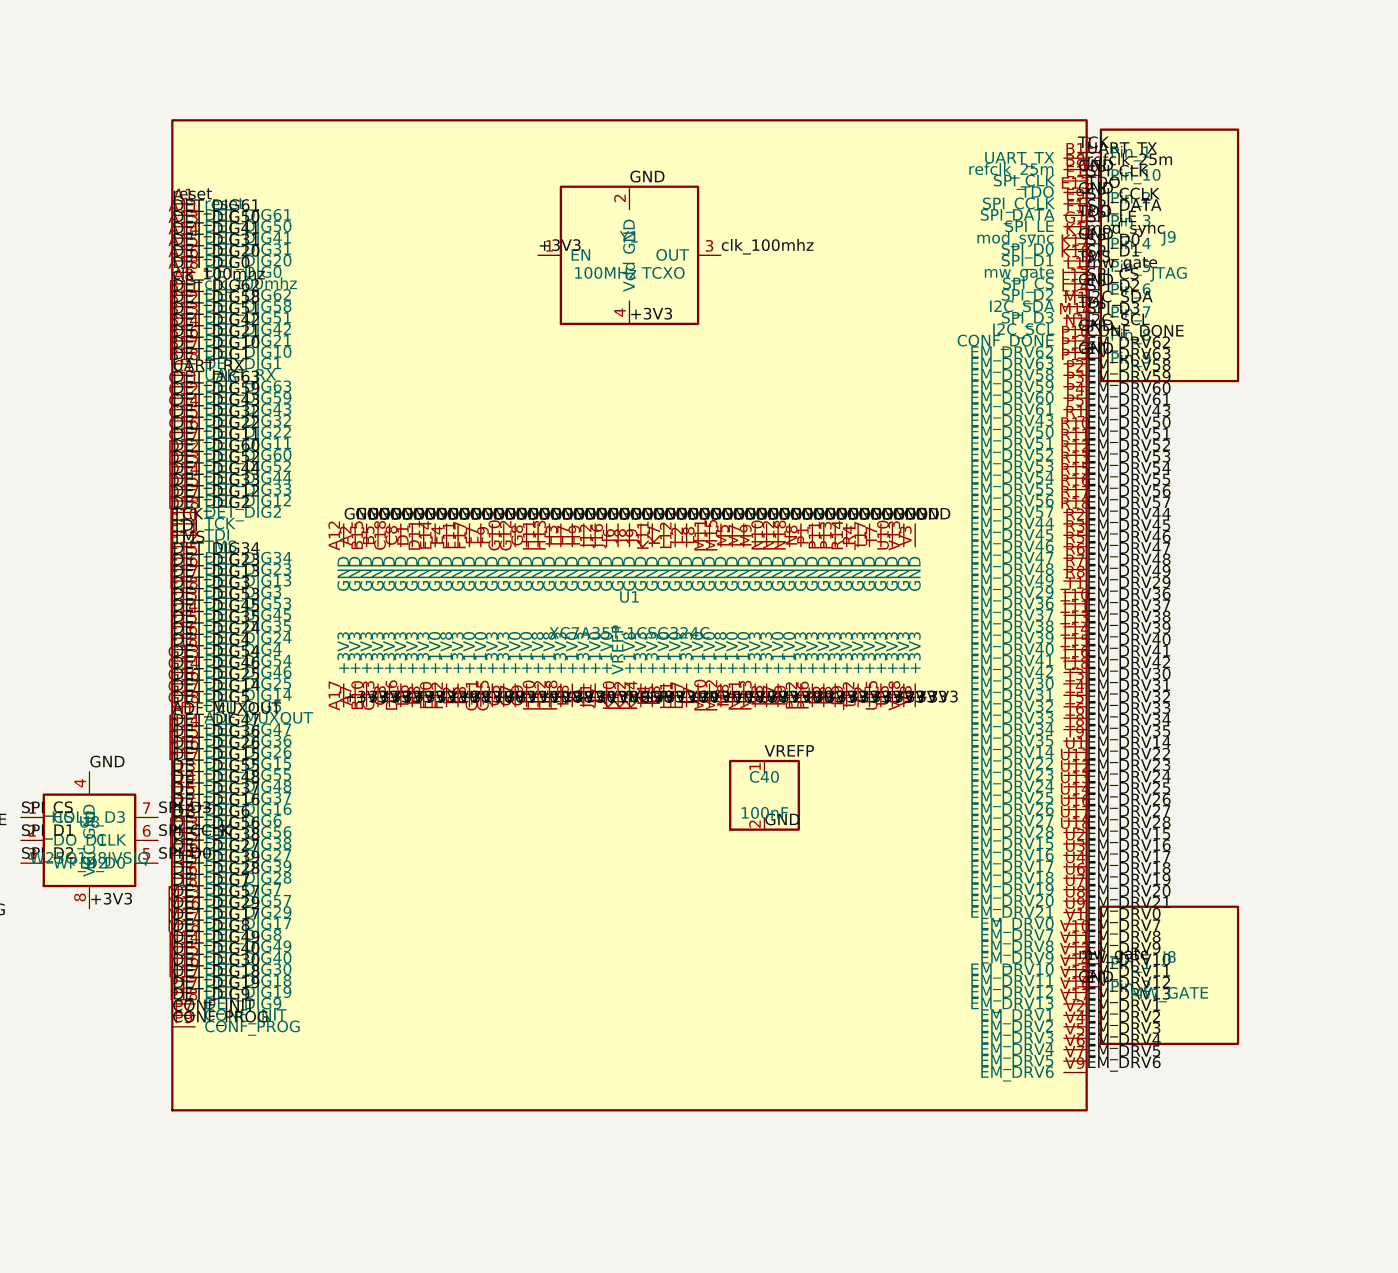
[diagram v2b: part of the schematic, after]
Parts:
- removed U1: XC7A35T-1CPG236C, Package_BGA:Xilinx_CPG236, symbol qssc:XC7A35T_CPG236
- added U1: XC7A35T-1CSG324C, Package_BGA:Xilinx_CSG324, symbol qssc:XC7A35T_CSG324
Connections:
- net +1V0: now also U1.F10 (+1V0), U1.F8 (+1V0), U1.G11 (+1V0), U1.G7 (+1V0), U1.G9 (+1V0), U1.H8 (+1V0), U1.J11 (+1V0), U1.J7 (+1V0), U1.K8 (+1V0), U1.L11 (+1V0), U1.L7 (+1V0), U1.M10 (+1V0), U1.M8 (+1V0), U1.N11 (+1V0), U1.N7 (+1V0), U1.N9 (+1V0)
- net +1V8: now also U1.F12 (+1V8), U1.H10 (+1V8), U1.H12 (+1V8), U1.K12 (+1V8), U1.M12 (+1V8)
- net +3V3: now also U1.A17 (+3V3), U1.A7 (+3V3), U1.B10 (+3V3), U1.C13 (+3V3), U1.C3 (+3V3), U1.D16 (+3V3), U1.D6 (+3V3), U1.E8 (+3V3), U1.F2 (+3V3), U1.G15 (+3V3), U1.G5 (+3V3), U1.H18 (+3V3), U1.J1 (+3V3), U1.K14 (+3V3), U1.K4 (+3V3), U1.L17 (+3V3), U1.N13 (+3V3), U1.N3 (+3V3), U1.P12 (+3V3), U1.P16 (+3V3), U1.P6 (+3V3), U1.P8 (+3V3), U1.R9 (+3V3), U1.T12 (+3V3), U1.T2 (+3V3), U1.U15 (+3V3), U1.U5 (+3V3), U1.V18 (+3V3), U1.V8 (+3V3)
- net ADF_MUXOUT: now also U1.H1 (ADF_MUXOUT)
- net CONF_DONE: now also U1.P10 (CONF_DONE)
- net CONF_INIT: now also U1.P7 (CONF_INIT)
- net CONF_PROG: now also U1.P9 (CONF_PROG)
- net DET_DIG0: now also U1.A18 (DET_DIG0)
- net DET_DIG1: now also U1.B18 (DET_DIG1)
- net DET_DIG10: now also U1.B17 (DET_DIG10)
- net DET_DIG11: now also U1.C17 (DET_DIG11)
- net DET_DIG12: now also U1.D17 (DET_DIG12)
- net DET_DIG13: now also U1.E17 (DET_DIG13)
- net DET_DIG14: now also U1.G17 (DET_DIG14)
- net DET_DIG15: now also U1.H17 (DET_DIG15)
- net DET_DIG16: now also U1.J17 (DET_DIG16)
- net DET_DIG17: now also U1.M17 (DET_DIG17)
- net DET_DIG18: now also U1.N17 (DET_DIG18)
- net DET_DIG19: now also U1.P17 (DET_DIG19)
- net DET_DIG2: now also U1.D18 (DET_DIG2)
- net DET_DIG20: now also U1.A16 (DET_DIG20)
- net DET_DIG21: now also U1.B16 (DET_DIG21)
- net DET_DIG22: now also U1.C16 (DET_DIG22)
- net DET_DIG23: now also U1.E16 (DET_DIG23)
- net DET_DIG24: now also U1.F16 (DET_DIG24)
- net DET_DIG25: now also U1.G16 (DET_DIG25)
- net DET_DIG26: now also U1.H16 (DET_DIG26)
- net DET_DIG27: now also U1.K16 (DET_DIG27)
- net DET_DIG28: now also U1.L16 (DET_DIG28)
- net DET_DIG29: now also U1.M16 (DET_DIG29)
- net DET_DIG3: now also U1.E18 (DET_DIG3)
- net DET_DIG30: now also U1.N16 (DET_DIG30)
- net DET_DIG31: now also U1.A15 (DET_DIG31)
- net DET_DIG32: now also U1.C15 (DET_DIG32)
- net DET_DIG33: now also U1.D15 (DET_DIG33)
- net DET_DIG34: now also U1.E15 (DET_DIG34)
- net DET_DIG35: now also U1.F15 (DET_DIG35)
- net DET_DIG36: now also U1.H15 (DET_DIG36)
- net DET_DIG37: now also U1.J15 (DET_DIG37)
- net DET_DIG38: now also U1.K15 (DET_DIG38)
- net DET_DIG39: now also U1.L15 (DET_DIG39)
- net DET_DIG4: now also U1.F18 (DET_DIG4)
- net DET_DIG40: now also U1.N15 (DET_DIG40)
- net DET_DIG41: now also U1.A14 (DET_DIG41)
- net DET_DIG42: now also U1.B14 (DET_DIG42)
- net DET_DIG43: now also U1.C14 (DET_DIG43)
- net DET_DIG44: now also U1.D14 (DET_DIG44)
- net DET_DIG45: now also U1.F14 (DET_DIG45)
- net DET_DIG46: now also U1.G14 (DET_DIG46)
- net DET_DIG47: now also U1.H14 (DET_DIG47)
- net DET_DIG48: now also U1.J14 (DET_DIG48)
- net DET_DIG49: now also U1.N14 (DET_DIG49)
- net DET_DIG5: now also U1.G18 (DET_DIG5)
- net DET_DIG50: now also U1.A13 (DET_DIG50)
- net DET_DIG51: now also U1.B13 (DET_DIG51)
- net DET_DIG52: now also U1.D13 (DET_DIG52)
- net DET_DIG53: now also U1.F13 (DET_DIG53)
- net DET_DIG54: now also U1.G13 (DET_DIG54)
- net DET_DIG55: now also U1.J13 (DET_DIG55)
- net DET_DIG56: now also U1.K13 (DET_DIG56)
- net DET_DIG57: now also U1.M13 (DET_DIG57)
- net DET_DIG58: now also U1.B12 (DET_DIG58)
- net DET_DIG59: now also U1.C12 (DET_DIG59)
- net DET_DIG6: now also U1.J18 (DET_DIG6)
- net DET_DIG60: now also U1.D12 (DET_DIG60)
- net DET_DIG61: now also U1.A11 (DET_DIG61)
- net DET_DIG62: now also U1.B11 (DET_DIG62)
- net DET_DIG63: now also U1.C11 (DET_DIG63)
- net DET_DIG7: now also U1.L18 (DET_DIG7)
- net DET_DIG8: now also U1.M18 (DET_DIG8)
- net DET_DIG9: now also U1.P18 (DET_DIG9)
- net EM_DRV0: now also U1.V1 (EM_DRV0)
- net EM_DRV1: now also U1.V2 (EM_DRV1)
- net EM_DRV10: now also U1.V14 (EM_DRV10)
- net EM_DRV11: now also U1.V15 (EM_DRV11)
- net EM_DRV12: now also U1.V16 (EM_DRV12)
- net EM_DRV13: now also U1.V17 (EM_DRV13)
- net EM_DRV14: now also U1.U1 (EM_DRV14)
- net EM_DRV15: now also U1.U2 (EM_DRV15)
- net EM_DRV16: now also U1.U3 (EM_DRV16)
- net EM_DRV17: now also U1.U4 (EM_DRV17)
- net EM_DRV18: now also U1.U6 (EM_DRV18)
- net EM_DRV19: now also U1.U7 (EM_DRV19)
- net EM_DRV2: now also U1.V4 (EM_DRV2)
- net EM_DRV20: now also U1.U8 (EM_DRV20)
- net EM_DRV21: now also U1.U9 (EM_DRV21)
- net EM_DRV22: now also U1.U11 (EM_DRV22)
- net EM_DRV23: now also U1.U12 (EM_DRV23)
- net EM_DRV24: now also U1.U13 (EM_DRV24)
- net EM_DRV25: now also U1.U14 (EM_DRV25)
- net EM_DRV26: now also U1.U16 (EM_DRV26)
- net EM_DRV27: now also U1.U17 (EM_DRV27)
- net EM_DRV28: now also U1.U18 (EM_DRV28)
- net EM_DRV29: now also U1.T1 (EM_DRV29)
- net EM_DRV3: now also U1.V5 (EM_DRV3)
- net EM_DRV30: now also U1.T3 (EM_DRV30)
- net EM_DRV31: now also U1.T4 (EM_DRV31)
- net EM_DRV32: now also U1.T5 (EM_DRV32)
- net EM_DRV33: now also U1.T6 (EM_DRV33)
- net EM_DRV34: now also U1.T8 (EM_DRV34)
- net EM_DRV35: now also U1.T9 (EM_DRV35)
- net EM_DRV36: now also U1.T10 (EM_DRV36)
- net EM_DRV37: now also U1.T11 (EM_DRV37)
- net EM_DRV38: now also U1.T13 (EM_DRV38)
- net EM_DRV39: now also U1.T14 (EM_DRV39)
- net EM_DRV4: now also U1.V6 (EM_DRV4)
- net EM_DRV40: now also U1.T15 (EM_DRV40)
- net EM_DRV41: now also U1.T16 (EM_DRV41)
- net EM_DRV42: now also U1.T18 (EM_DRV42)
- net EM_DRV43: now also U1.R1 (EM_DRV43)
- net EM_DRV44: now also U1.R2 (EM_DRV44)
- net EM_DRV45: now also U1.R3 (EM_DRV45)
- net EM_DRV46: now also U1.R5 (EM_DRV46)
- net EM_DRV47: now also U1.R6 (EM_DRV47)
- net EM_DRV48: now also U1.R7 (EM_DRV48)
- net EM_DRV49: now also U1.R8 (EM_DRV49)
- net EM_DRV5: now also U1.V7 (EM_DRV5)
- net EM_DRV50: now also U1.R10 (EM_DRV50)
- net EM_DRV51: now also U1.R11 (EM_DRV51)
- net EM_DRV52: now also U1.R12 (EM_DRV52)
- net EM_DRV53: now also U1.R13 (EM_DRV53)
- net EM_DRV54: now also U1.R15 (EM_DRV54)
- net EM_DRV55: now also U1.R16 (EM_DRV55)
- net EM_DRV56: now also U1.R17 (EM_DRV56)
- net EM_DRV57: now also U1.R18 (EM_DRV57)
- net EM_DRV58: now also U1.P2 (EM_DRV58)
- net EM_DRV59: now also U1.P3 (EM_DRV59)
- net EM_DRV6: now also U1.V9 (EM_DRV6)
- net EM_DRV60: now also U1.P4 (EM_DRV60)
- net EM_DRV61: now also U1.P5 (EM_DRV61)
- net EM_DRV62: now also U1.P14 (EM_DRV62)
- net EM_DRV63: now also U1.P15 (EM_DRV63)
- net EM_DRV7: now also U1.V10 (EM_DRV7)
- net EM_DRV8: now also U1.V11 (EM_DRV8)
- net EM_DRV9: now also U1.V12 (EM_DRV9)
- net GND: now also U1.A12 (GND), U1.A2 (GND), U1.B15 (GND), U1.B5 (GND), U1.C18 (GND), U1.C8 (GND), U1.D1 (GND), U1.D11 (GND), U1.E14 (GND), U1.E4 (GND), U1.F11 (GND), U1.F17 (GND), U1.F7 (GND), U1.F9 (GND), U1.G10 (GND), U1.G12 (GND), U1.G8 (GND), U1.H11 (GND), U1.H13 (GND), U1.H3 (GND), U1.H7 (GND), U1.H9 (GND), U1.J12 (GND), U1.J16 (GND), U1.J6 (GND), U1.J8 (GND), U1.J9 (GND), U1.K11 (GND), U1.K7 (GND), U1.L12 (GND), U1.L2 (GND), U1.L8 (GND), U1.M11 (GND), U1.M15 (GND), U1.M5 (GND), U1.M7 (GND), U1.M9 (GND), U1.N10 (GND), U1.N12 (GND), U1.N18 (GND), U1.N8 (GND), U1.P1 (GND), U1.P11 (GND), U1.P13 (GND), U1.R14 (GND), U1.R4 (GND), U1.T17 (GND), U1.T7 (GND), U1.U10 (GND), U1.V13 (GND), U1.V3 (GND)
- net I2C_SCL: now also U1.N1 (I2C_SCL)
- net I2C_SDA: now also U1.M1 (I2C_SDA)
- net SPI_CCLK: now also U1.E9 (SPI_CCLK)
- net SPI_CLK: now also U1.E1 (SPI_CLK)
- net SPI_CS: now also U1.L13 (SPI_CS)
- net SPI_D0: now also U1.K17 (SPI_D0)
- net SPI_D1: now also U1.K18 (SPI_D1)
- net SPI_D2: now also U1.L14 (SPI_D2)
- net SPI_D3: now also U1.M14 (SPI_D3)
- net SPI_DATA: now also U1.F1 (SPI_DATA)
- net SPI_LE: now also U1.G1 (SPI_LE)
- net TCK: now also U1.E10 (TCK)
- net TDI: now also U1.E11 (TDI)
- net TDO: now also U1.E13 (TDO)
- net TMS: now also U1.E12 (TMS)
- net UART_RX: now also U1.C1 (UART_RX)
- net UART_TX: now also U1.B1 (UART_TX)
- net VREFP: now also U1.K10 (VREFP)
- net clk_100mhz: now also U1.A8 (clk_100mhz)
- net mod_sync: now also U1.K1 (mod_sync)
- net mw_gate: now also U1.L1 (mw_gate)
- net refclk_25m: now also U1.B8 (refclk_25m)
- net reset: now also U1.A1 (reset)
